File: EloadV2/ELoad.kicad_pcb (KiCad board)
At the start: 4 copper layers, 170.2 x 94 mm, 127 parts, among them J1 Power Input, J2 Conn_01x02, J3 OLED, J4 ENCODER, J5 SWDEBUG, M1 Fan_4pin, Q1 Q_PMOS_GSD, Q2 Q_NPN_BEC, Q3 Q_NPN_BEC, Q4 Q_NMOS_GDS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

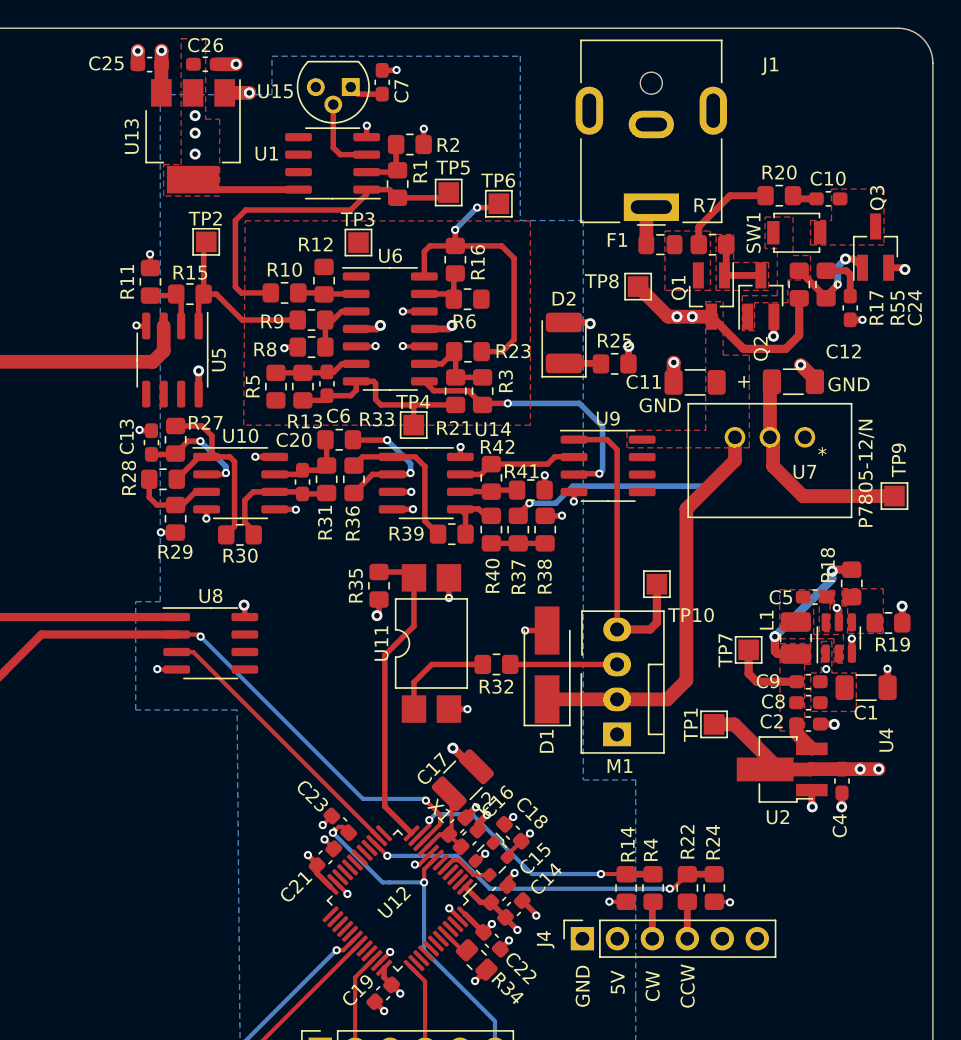
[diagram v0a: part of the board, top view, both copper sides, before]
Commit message: removing power, waveform generation, op amp pi, button latch
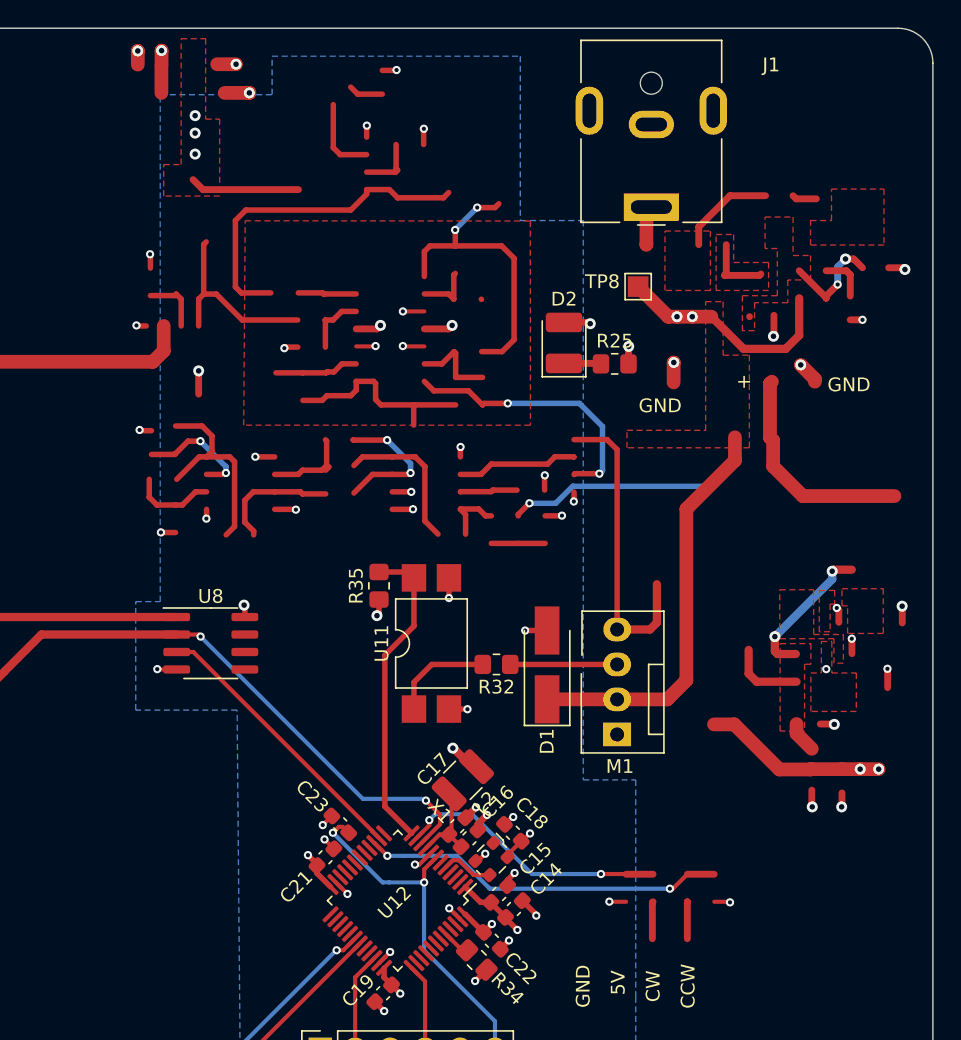
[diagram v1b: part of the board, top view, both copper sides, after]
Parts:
- removed C1, C11, C12: 10u, Capacitor_SMD:C_1206_3216Metric_Pad1.33x1.80mm_HandSolder
- removed C10, C6: 1u, Capacitor_SMD:C_0603_1608Metric_Pad1.08x0.95mm_HandSolder
- removed C13: 0.01u, Capacitor_SMD:C_0603_1608Metric_Pad1.08x0.95mm_HandSolder
- removed C2, C25: 10u, Capacitor_SMD:C_0603_1608Metric_Pad1.08x0.95mm_HandSolder
- removed C20, C24: 10n, Capacitor_SMD:C_0603_1608Metric_Pad1.08x0.95mm_HandSolder
- removed C26, C4, C8, C9: 22u, Capacitor_SMD:C_0603_1608Metric_Pad1.08x0.95mm_HandSolder
- removed C5: 100n, Capacitor_SMD:C_0603_1608Metric_Pad1.08x0.95mm_HandSolder
- removed C7: 0.1u, Capacitor_SMD:C_0603_1608Metric_Pad1.08x0.95mm_HandSolder
- removed F1: Fuse, Fuse:Fuse_0805_2012Metric_Pad1.15x1.40mm_HandSolder
- removed J4: ENCODER, Connector_PinSocket_2.54mm:PinSocket_1x06_P2.54mm_Vertical
- removed L1: 2.2u, Inductor_SMD:L_1008_2520Metric_Pad1.43x2.20mm_HandSolder
- removed Q1: Q_PMOS_GSD, Package_TO_SOT_SMD:SOT-23_Handsoldering
- removed Q2, Q3: Q_NPN_BEC, Package_TO_SOT_SMD:SOT-23_Handsoldering
- removed R1, R15: 70k, Resistor_SMD:R_0805_2012Metric_Pad1.20x1.40mm_HandSolder
- removed R10, R11, R12, R19, R2, R21, R23, R28, R29, R3, R33, R37, R38, R5, R6, R8, R9: 10k, Resistor_SMD:R_0805_2012Metric_Pad1.20x1.40mm_HandSolder
- removed R13: 8k, Resistor_SMD:R_0805_2012Metric_Pad1.20x1.40mm_HandSolder
- removed R14, R24: 3.3k, Resistor_SMD:R_0805_2012Metric_Pad1.20x1.40mm_HandSolder
- removed R16: 20k, Resistor_SMD:R_0805_2012Metric_Pad1.20x1.40mm_HandSolder
- removed R17, R31, R7: 100k, Resistor_SMD:R_0805_2012Metric_Pad1.20x1.40mm_HandSolder
- removed R18: 52.3k, Resistor_SMD:R_0805_2012Metric_Pad1.20x1.40mm_HandSolder
- removed R20: 1M, Resistor_SMD:R_0805_2012Metric_Pad1.20x1.40mm_HandSolder
- removed R22, R4: 1.7k, Resistor_SMD:R_0805_2012Metric_Pad1.20x1.40mm_HandSolder
- removed R27, R36: 5k, Resistor_SMD:R_0805_2012Metric_Pad1.20x1.40mm_HandSolder
- removed R30: 2.5k, Resistor_SMD:R_0805_2012Metric_Pad1.20x1.40mm_HandSolder
- removed R39, R40, R41, R42, R55: 1k, Resistor_SMD:R_0805_2012Metric_Pad1.20x1.40mm_HandSolder
- removed SW1: SW_Push, Button_Switch_SMD:SW_SPST_B3U-1000P
- removed TP1, TP10, TP3, TP4, TP6, TP7, TP9: TestPoint_Probe, TestPoint:TestPoint_Pad_1.5x1.5mm
- removed TP2, TP5: Test, TestPoint:TestPoint_Pad_1.5x1.5mm
- removed U1, U10, U14, U5: TL072, Package_SO:SOIC-8_3.9x4.9mm_P1.27mm
- removed U13: AZ1117-5.0, Package_TO_SOT_SMD:SOT-223-3_TabPin2
- removed U15: MCP9700AT-ETT, Package_TO_SOT_THT:TO-92
- removed U2: AZ1117-3.3, Package_TO_SOT_SMD:SOT-89-3_Handsoldering
- removed U4: AP62250WU-7, Package_TO_SOT_SMD:TSOT-23-6
- removed U6: TL074, Package_SO:SOIC-14_3.9x8.7mm_P1.27mm
- removed U7: P7805-12/N, P7805-Q24-S12-S:P78E12-1000
- removed U9: LM393, Package_SO:SOIC-8_3.9x4.9mm_P1.27mm
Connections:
- J1 pad 1: Net-(F1-Pad1) -> unconnected-(J1-Pad1)
- J1 pad 2: GND -> unconnected-(J1-Pad2)
- U12 pad 11: /ROT_CW -> unconnected-(U12-Pad11)
- U12 pad 15: /ROT_CCW -> unconnected-(U12-Pad15)
- U8 pad 4: GND -> (no net)
- U8 pad 8: +5V -> (no net)
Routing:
- net (no net): track 0.00 -> 292.4 mm, vias 0 -> 15
- net unconnected-(U12-Pad15): track 0.00 -> 26.5 mm, vias 0 -> 2
- net /ROT_CCW: track 26.5 -> 0.00 mm, vias 2 -> 0
- net /ambient: track 24.6 -> 0.00 mm
- net /prop: track 22.6 -> 0.00 mm, vias 2 -> 0
- net -12V: track 20.3 -> 0.00 mm, vias 3 -> 0
- net unconnected-(U12-Pad11): track 0.00 -> 19.9 mm, vias 0 -> 2
- net /ROT_CW: track 19.9 -> 0.00 mm, vias 2 -> 0
- net /pidOUT: track 19.8 -> 0.00 mm, vias 2 -> 0
- net VDC: track 18.3 -> 0.00 mm, vias 2 -> 0
- net /squareout: track 15.2 -> 0.00 mm
- net /integrator: track 14.9 -> 0.00 mm
- net /TEMP: track 13.9 -> 0.00 mm
- net /trihalfout: track 11.0 -> 0.00 mm
- net /trihalf-: track 10.3 -> 0.00 mm, vias 2 -> 0
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- added copper zone on F.Cu, net (none)
- added copper zone on In2.Cu, net (none)
- removed copper zone on In2.Cu, net -12V
- removed copper zone on F.Cu, net /BST
- removed copper zone on F.Cu, net /FB
- removed copper zone on F.Cu, net /SW
- removed copper zone on F.Cu, net /buttonBase
- removed copper zone on F.Cu, net /buttonCollector
- removed copper zone on F.Cu, net /buttonGate
- removed copper zone on F.Cu, net /error
- removed copper zone on F.Cu, net Net-(F1-Pad2)
- removed copper zone on F.Cu, net VDC
